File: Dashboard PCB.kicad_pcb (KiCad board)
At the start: 2 copper layers, 150 x 100.2 mm, 73 parts, among them J1 Controls_Leader_Export_02x06, J3 INDICATOR_SWITCH_OUT, J5 Horn_In_01x02, J6 Horn_Out_01x02, J8 Supp_Out, J9 Supp_In, Q1 TO200P800X182-5N, Q2 Q_PMOS_GDS

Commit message: stuff
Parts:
- renumbered BPS_HZD to BPS_HZD1
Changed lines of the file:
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@@
 		(at 120.3 108.6 -90)
 		(property "Reference" "GEAR_SW_12V1"
-			(at 0.02 3.94 270)
+			(at 0.02 3.94 -90)
 			(unlocked yes)
 			(layer "F.Fab")
@@
 		(descr "SMD rectangular pad as test Point, square 1.0mm side length")
 		(tags "test point SMD pad rectangle square")
-		(property "Reference" "BPS_HZD"
+		(property "Reference" "BPS_HZD1"
 			(at 0 1.448 0)
 			(layer "B.SilkS")
@@
 		)
 		(property "Value" "BZT52-B12-QX"
-			(at 0 0 360)
+			(at 0 0 0)
 			(layer "B.SilkS")
 			(hide yes)
@@
 		)
 		(property "Footprint" "Footprints:BZT52B12QX"
-			(at 0 0 360)
+			(at 0 0 0)
 			(layer "B.Fab")
 			(hide yes)
@@
 		)
 		(property "Datasheet" ""
-			(at 0 0 360)
+			(at 0 0 0)
 			(layer "B.Fab")
 			(hide yes)
@@
 		)
 		(property "Description" "Zener diode"
-			(at 0 0 360)
+			(at 0 0 0)
 			(layer "B.Fab")
 			(hide yes)
@@
 		)
 		(fp_text user "${REFERENCE}"
-			(at 0 0 360)
+			(at 0 0 0)
 			(layer "B.Fab")
 			(effects
@@
 		(tags "Fuse")
 		(property "Reference" "F1"
-			(at 0 0 360)
+			(at 0 0 0)
 			(layer "B.SilkS")
 			(effects
@@
 		)
 		(property "Value" "Fuse"
-			(at 0 0 360)
+			(at 0 0 0)
 			(layer "B.SilkS")
 			(hide yes)
@@
 		)
 		(fp_text user "${REFERENCE}"
-			(at 0 0 360)
+			(at 0 0 0)
 			(layer "B.Fab")
 			(effects

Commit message: fixed
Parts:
- turned LFT_LED1 to 180 degrees
- renumbered BPS_HZD1 to BPS_HZD, LV_EN1 to LV_EN, SUPP+1 to SUPP+, SUPP-1 to SUPP-
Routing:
- net GND: track 0.06 -> 0.00 mm, vias 4 -> 5
- net Net-(LFT_LED1-A): vias 2 -> 1
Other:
- board text added: "+"
- board text added: "-"
- board text added: "LV_EN"

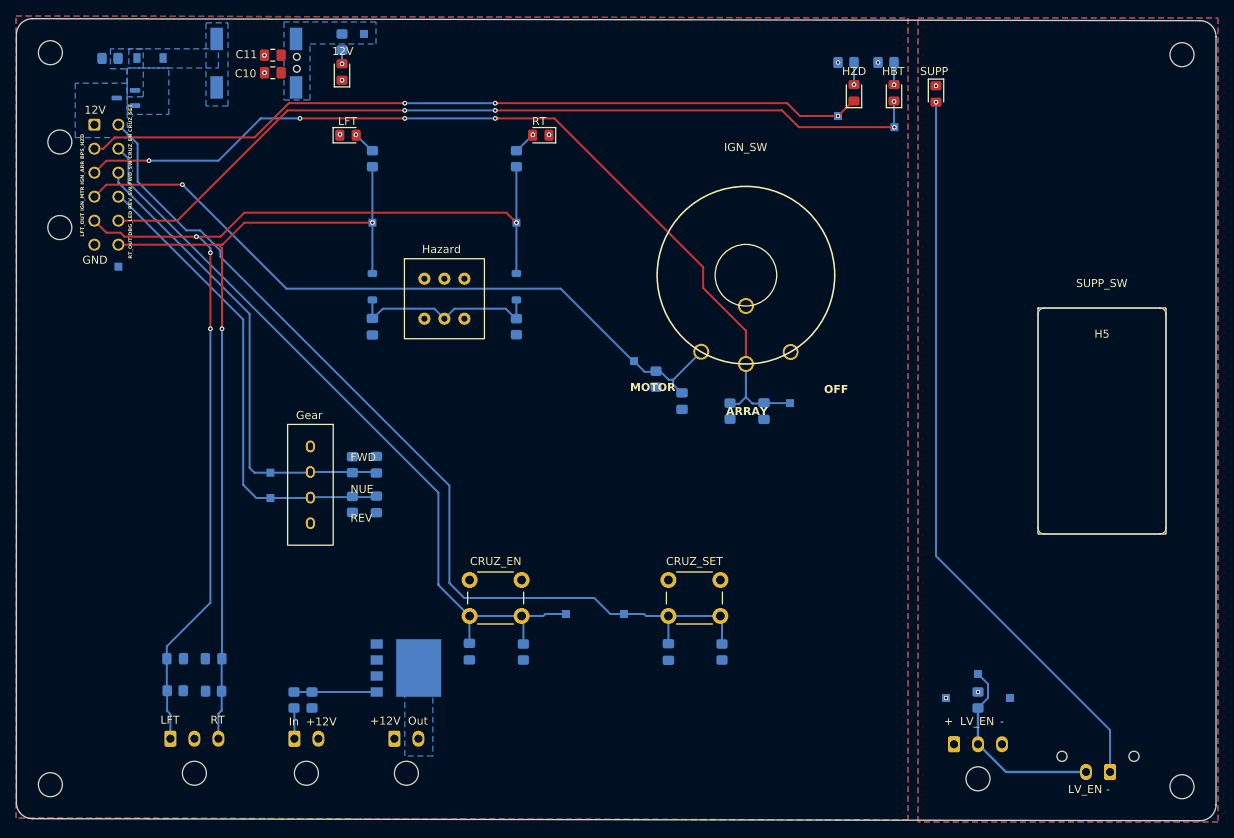
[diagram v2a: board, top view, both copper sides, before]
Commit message: added flyback and made supp hole bigger
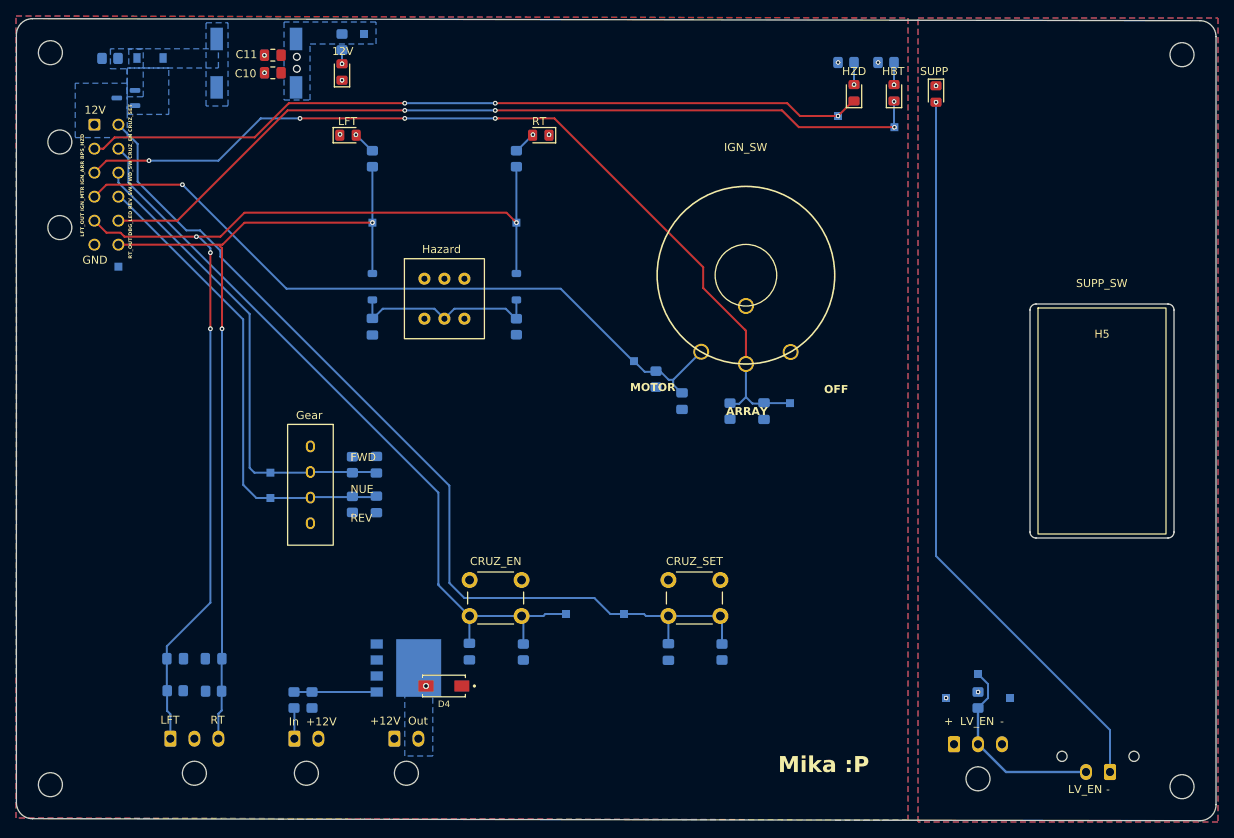
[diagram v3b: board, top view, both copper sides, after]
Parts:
- added D4: VSSAF522, Footprints:DO-221AC, F.Cu at (137.0, 133.8)
- R16: value 30k -> 1k
- moved G*** 1.27 mm to (155.2, 109.5)
- renumbered BPS_HZD to BPS_HZD1, LV_EN to LV_EN1, SUPP+ to SUPP+1, SUPP- to SUPP-1
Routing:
- net Net-(J6-Pin_2): vias 0 -> 1
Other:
- outline, holes or cut-outs redrawn
- board text added: "Mika :P"
